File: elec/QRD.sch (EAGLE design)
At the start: 10 parts, among them IC1 LM311D

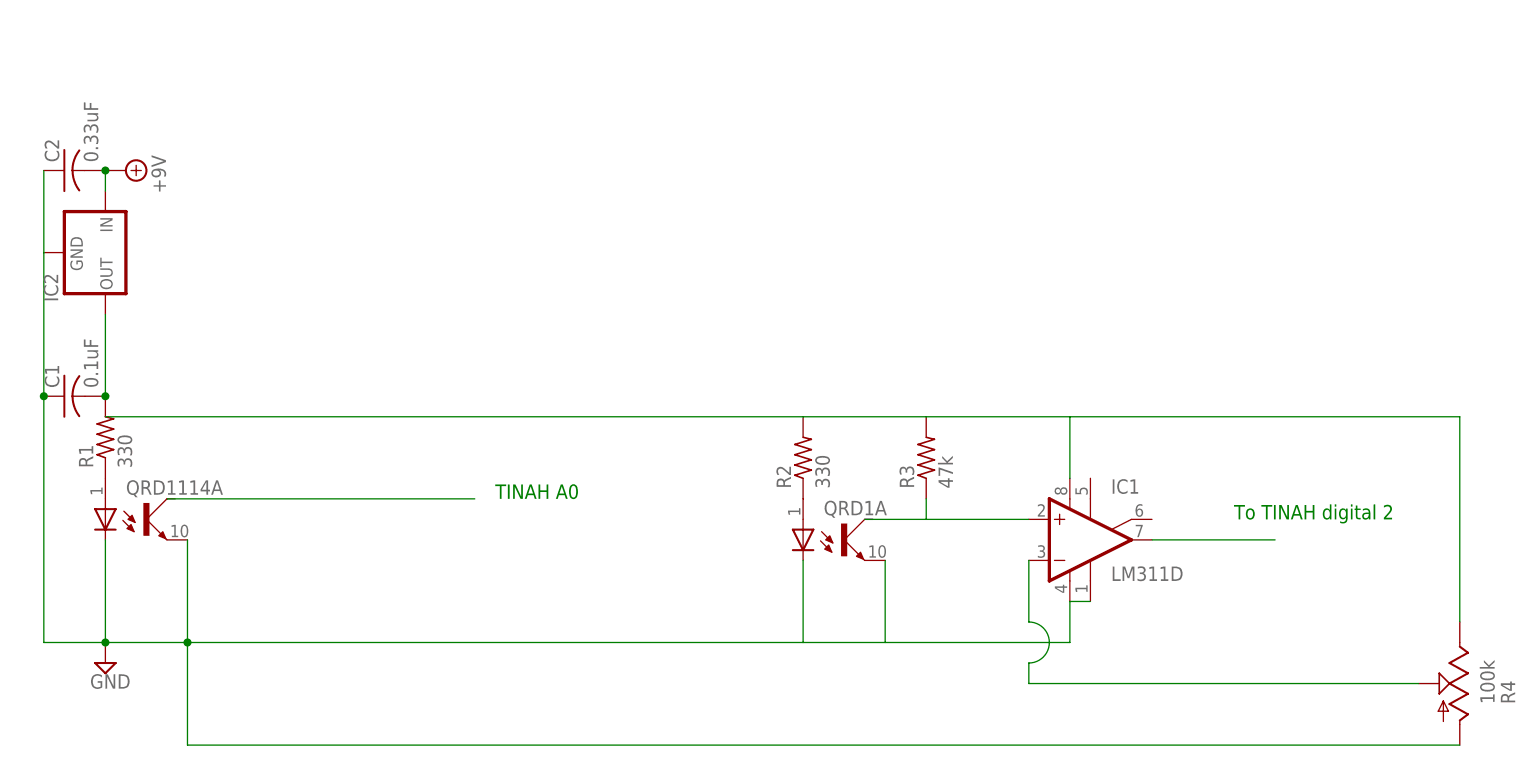
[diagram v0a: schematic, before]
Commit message: Circuit pictures for website added
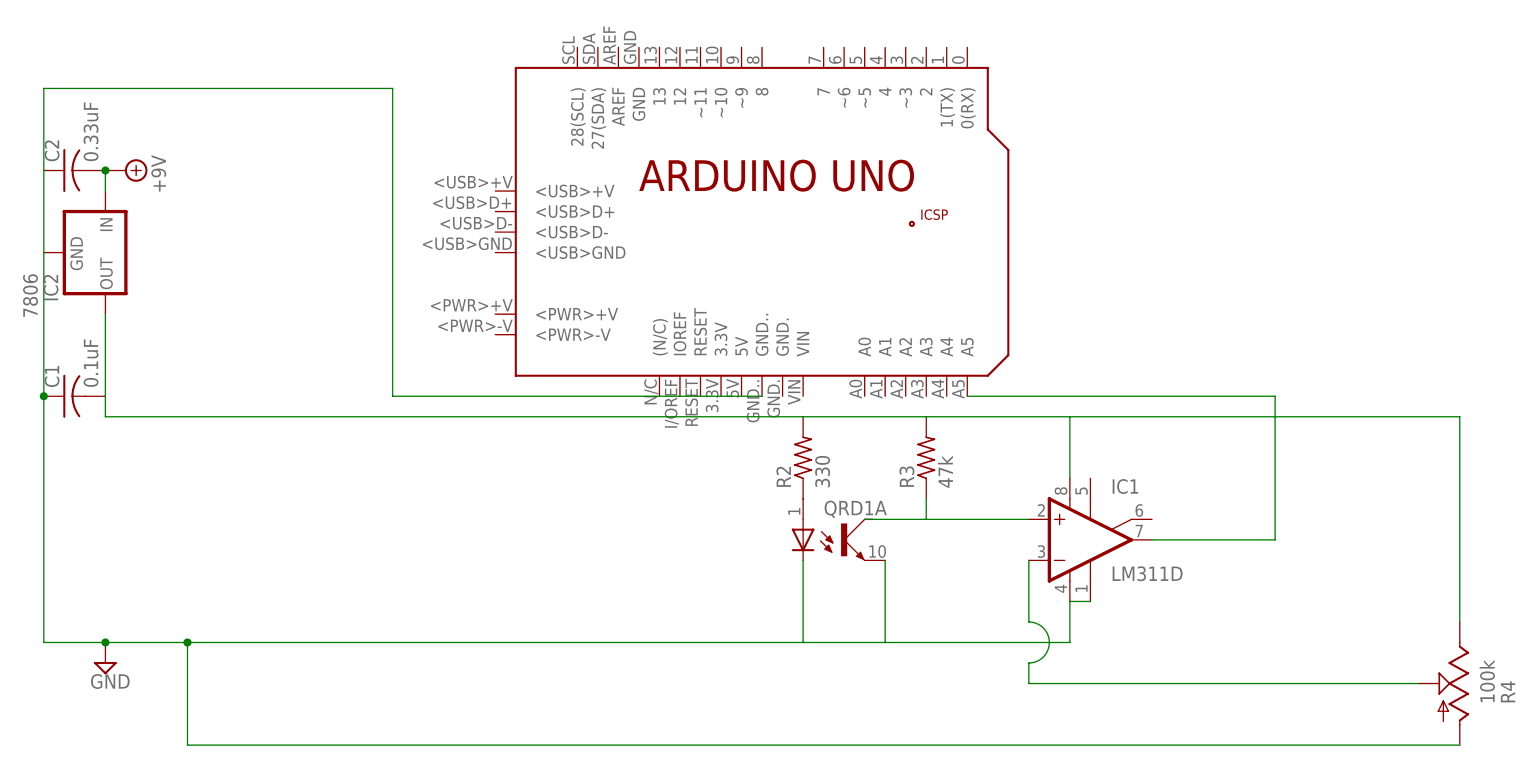
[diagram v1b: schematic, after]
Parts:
- removed QRD1114: SFH6943, opto-vishay:SFH6943
- removed R1: 330, resistor:R-US_0204/2V
- added PCB1: ARDUINO_UNO, E14_Arduino_revB:ARDUINO_UNO
- IC2: value (none) -> 7806
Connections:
- removed net N$2: QRD1114A.A, R1.1
- removed net N$7: IC1.OUT
- removed net N$8: C1.2, IC2.OUT, R1.2
- new net N$1: IC1.OUT, PCB1.A5
- net GND: now also PCB1.GND..; no longer QRD1114A.EMI
- net N$6: now also C1.2, IC2.OUT
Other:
- note removed: "TINAH A0"
- note removed: "To TINAH digital 2"
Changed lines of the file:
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@@
 <layer number="48" name="Document" color="7" fill="1" visible="no" active="no"/>
 <layer number="49" name="Reference" color="7" fill="1" visible="no" active="no"/>
+<layer number="50" name="dxf" color="7" fill="1" visible="no" active="no"/>
 <layer number="51" name="tDocu" color="6" fill="1" visible="no" active="no"/>
 <layer number="52" name="bDocu" color="7" fill="1" visible="no" active="no"/>
+<layer number="53" name="tGND_GNDA" color="7" fill="9" visible="no" active="no"/>
+<layer number="54" name="bGND_GNDA" color="1" fill="9" visible="no" active="no"/>
+<layer number="56" name="wert" color="7" fill="1" visible="no" active="no"/>
 <layer number="57" name="t3D" color="6" fill="5" visible="no" active="no"/>
 <layer number="58" name="b3D" color="5" fill="4" visible="no" active="no"/>
@@
 <layer number="98" name="Guide" color="6" fill="1" visible="yes" active="yes"/>
 <layer number="99" name="SpiceOrder" color="5" fill="1" visible="yes" active="yes"/>
+<layer number="100" name="Muster" color="7" fill="1" visible="no" active="no"/>
+<layer number="101" name="Patch_Top" color="12" fill="4" visible="yes" active="yes"/>
+<layer number="102" name="Vscore" color="7" fill="1" visible="yes" active="yes"/>
+<layer number="103" name="tMap" color="7" fill="1" visible="yes" active="yes"/>
+<layer number="104" name="Name" color="16" fill="1" visible="yes" active="yes"/>
+<layer number="105" name="tPlate" color="7" fill="1" visible="yes" active="yes"/>
+<layer number="106" name="bPlate" color="7" fill="1" visible="yes" active="yes"/>
+<layer number="107" name="Crop" color="7" fill="1" visible="yes" active="yes"/>
+<layer number="116" name="Patch_BOT" color="9" fill="4" visible="yes" active="yes"/>
+<layer number="121" name="_tsilk" color="7" fill="1" visible="yes" active="yes"/>
+<layer number="122" name="_bsilk" color="7" fill="1" visible="yes" active="yes"/>
+<layer number="125" name="_tNames" color="7" fill="1" visible="yes" active="yes"/>
+<layer number="144" name="Drill_legend" color="7" fill="1" visible="yes" active="yes"/>
+<layer number="151" name="HeatSink" color="7" fill="1" visible="yes" active="yes"/>
+<layer number="200" name="200bmp" color="1" fill="10" visible="yes" active="yes"/>
+<layer number="201" name="201bmp" color="2" fill="10" visible="yes" active="yes"/>
+<layer number="202" name="202bmp" color="3" fill="10" visible="yes" active="yes"/>
+<layer number="203" name="203bmp" color="4" fill="10" visible="yes" active="yes"/>
+<layer number="204" name="204bmp" color="5" fill="10" visible="yes" active="yes"/>
+<layer number="205" name="205bmp" color="6" fill="10" visible="yes" active="yes"/>
+<layer number="206" name="206bmp" color="7" fill="10" visible="yes" active="yes"/>
+<layer number="207" name="207bmp" color="8" fill="10" visible="yes" active="yes"/>
+<layer number="208" name="208bmp" color="9" fill="10" visible="yes" active="yes"/>
+<layer number="209" name="209bmp" color="7" fill="1" visible="yes" active="yes"/>
+<layer number="210" name="210bmp" color="7" fill="1" visible="yes" active="yes"/>
+<layer number="211" name="211bmp" color="7" fill="1" visible="yes" active="yes"/>
+<layer number="212" name="212bmp" color="7" fill="1" visible="yes" active="yes"/>
+<layer number="213" name="213bmp" color="7" fill="1" visible="yes" active="yes"/>
+<layer number="214" name="214bmp" color="7" fill="1" visible="yes" active="yes"/>
+<layer number="215" name="215bmp" color="7" fill="1" visible="yes" active="yes"/>
+<layer number="216" name="216bmp" color="7" fill="1" visible="yes" active="yes"/>
+<layer number="217" name="217bmp" color="18" fill="1" visible="no" active="no"/>
+<layer number="218" name="218bmp" color="19" fill="1" visible="no" active="no"/>
+<layer number="219" name="219bmp" color="20" fill="1" visible="no" active="no"/>
+<layer number="220" name="220bmp" color="21" fill="1" visible="no" active="no"/>
+<layer number="221" name="221bmp" color="22" fill="1" visible="no" active="no"/>
+<layer number="222" name="222bmp" color="23" fill="1" visible="no" active="no"/>
+<layer number="223" name="223bmp" color="24" fill="1" visible="no" active="no"/>
+<layer number="224" name="224bmp" color="25" fill="1" visible="no" active="no"/>
+<layer number="250" name="Descript" color="3" fill="1" visible="no" active="no"/>
+<layer number="251" name="SMDround" color="12" fill="11" visible="no" active="no"/>
+<layer number="254" name="cooling" color="7" fill="1" visible="yes" active="yes"/>
 </layers>
 <schematic xreflabel="%F%N/%S.%C%R" xrefpart="/%S.%C%R">
@@
 </classes>
 <parts>
-<part name="QRD1114" library="opto-vishay" deviceset="SFH6943" device="" value=""/>
 <part name="SUPPLY1" library="supply2" deviceset="GND" device=""/>
-<part name="R1" library="resistor" deviceset="R-US_" device="0204/2V" value="330"/>
 <part name="R2" library="resistor" deviceset="R-US_" device="0204/2V" value="330"/>
 <part name="QRD1" library="opto-vishay" deviceset="SFH6943" device="" value=""/>
@@
 <part name="IC1" library="linear" deviceset="LM311" device="D"/>
 <part name="R4" library="pot" deviceset="TRIM_US-" device="3223G" value="100k"/>
-<part name="IC2" library="v-reg" deviceset="78XXL" device=""/>
+<part name="IC2" library="v-reg" deviceset="78XXL" device="" value="7806"/>
 <part name="C1" library="resistor" deviceset="C-US" device="025-024X044" value="0.1uF"/>
 <part name="C2" library="resistor" deviceset="C-US" device="025-024X044" value="0.33uF"/>
 <part name="SUPPLY2" library="supply2" deviceset="+9V" device=""/>
+<part name="PCB1" library="E14_Arduino_revB" deviceset="ARDUINO_UNO" device=""/>
 </parts>
 <sheets>
 <sheet>
 <plain>
-<text x="20.32" y="86.36" size="1.778" layer="91">TINAH A0</text>
-<text x="111.76" y="83.82" size="1.778" layer="91">To TINAH digital 2</text>
 </plain>
 <instances>
-<instance part="QRD1114" gate="A" x="-27.94" y="83.82"/>
 <instance part="SUPPLY1" gate="GND" x="-27.94" y="66.04"/>
-<instance part="R1" gate="G$1" x="-27.94" y="93.98" rot="R90"/>
 <instance part="R2" gate="G$1" x="58.42" y="91.44" rot="R90"/>
 <instance part="QRD1" gate="A" x="58.42" y="81.28"/>
@@
 <instance part="C2" gate="G$1" x="-33.02" y="127" rot="R90"/>
 <instance part="SUPPLY2" gate="G$1" x="-25.4" y="127" rot="R270"/>
+<instance part="PCB1" gate="G$1" x="53.34" y="121.92"/>
 </instances>
 <busses>
 </busses>
 <nets>
-<net name="N$1" class="0">
-<segment>
-<wire x1="-20.32" y1="86.36" x2="17.78" y2="86.36" width="0.1524" layer="91"/>
-</segment>
-</net>
 <net name="GND" class="0">
 <segment>
 <pinref part="SUPPLY1" gate="GND" pin="GND"/>
-<wire x1="-27.94" y1="81.28" x2="-27.94" y2="68.58" width="0.1524" layer="91"/>
-<pinref part="QRD1114" gate="A" pin="EMI"/>
 <wire x1="-27.94" y1="68.58" x2="-17.78" y2="68.58" width="0.1524" layer="91"/>
-<wire x1="-17.78" y1="68.58" x2="-17.78" y2="81.28" width="0.1524" layer="91"/>
 <wire x1="58.42" y1="78.74" x2="58.42" y2="68.58" width="0.1524" layer="91"/>
 <wire x1="58.42" y1="68.58" x2="-17.78" y2="68.58" width="0.1524" layer="91"/>
@@
 <pinref part="C2" gate="G$1" pin="1"/>
 <wire x1="-35.56" y1="127" x2="-35.56" y2="116.84" width="0.1524" layer="91"/>
-</segment>
-</net>
-<net name="N$2" class="0">
-<segment>
-<pinref part="QRD1114" gate="A" pin="A"/>
-<pinref part="R1" gate="G$1" pin="1"/>
+<wire x1="-35.56" y1="127" x2="-35.56" y2="137.16" width="0.1524" layer="91"/>
+<wire x1="-35.56" y1="137.16" x2="7.62" y2="137.16" width="0.1524" layer="91"/>
+<wire x1="7.62" y1="137.16" x2="7.62" y2="99.06" width="0.1524" layer="91"/>
+<pinref part="PCB1" gate="G$1" pin="GND.."/>
+<wire x1="7.62" y1="99.06" x2="53.34" y2="99.06" width="0.1524" layer="91"/>
 </segment>
 </net>
@@
 <wire x1="134.62" y1="63.5" x2="86.36" y2="63.5" width="0.1524" layer="91"/>
 <wire x1="86.36" y1="63.5" x2="86.36" y2="66.04" width="0.1524" layer="91"/>
-</segment>
-</net>
-<net name="N$7" class="0">
-<segment>
-<pinref part="IC1" gate="A" pin="OUT"/>
-<wire x1="101.6" y1="81.28" x2="116.84" y2="81.28" width="0.1524" layer="91"/>
 </segment>
 </net>
@@
 <wire x1="139.7" y1="71.12" x2="139.7" y2="96.52" width="0.1524" layer="91"/>
 <wire x1="139.7" y1="96.52" x2="91.44" y2="96.52" width="0.1524" layer="91"/>
-</segment>
-</net>
-<net name="N$8" class="0">
-<segment>
-<pinref part="R1" gate="G$1" pin="2"/>
 <pinref part="IC2" gate="A" pin="OUT"/>
 <wire x1="-27.94" y1="109.22" x2="-27.94" y2="99.06" width="0.1524" layer="91"/>
 <pinref part="C1" gate="G$1" pin="2"/>
-<junction x="-27.94" y="99.06"/>
+<wire x1="-27.94" y1="96.52" x2="-27.94" y2="99.06" width="0.1524" layer="91"/>
 </segment>
 </net>
@@
 </segment>
 </net>
+<net name="N$1" class="0">
+<segment>
+<pinref part="IC1" gate="A" pin="OUT"/>
+<wire x1="101.6" y1="81.28" x2="116.84" y2="81.28" width="0.1524" layer="91"/>
+<wire x1="116.84" y1="81.28" x2="116.84" y2="99.06" width="0.1524" layer="91"/>
+<pinref part="PCB1" gate="G$1" pin="A5"/>
+<wire x1="116.84" y1="99.06" x2="78.74" y2="99.06" width="0.1524" layer="91"/>
+</segment>
+</net>
